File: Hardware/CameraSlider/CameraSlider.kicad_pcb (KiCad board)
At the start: 2 copper layers, 100 x 50 mm, 19 parts, among them J1 Screw_Terminal_01x02, J10 Conn_01x04_Male, J11 Conn_01x04_Male, J2 Conn_01x02_Male, J3 Conn_01x03_Male, J4 Conn_01x02_Male, J5 Conn_01x02_Male, J6 Conn_01x03_Male, J7 Conn_01x03_Male, J8 Conn_02x03_Odd_Even, J9 Conn_01x04_Male, U1 A000005, U2 A4988_STEPPER_MOTOR_DRIVER_CA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

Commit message: Layout hinzugefügt
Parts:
- moved C1 8.52 mm to (165.1, 119.4), turned to 0 degrees
- moved R1 2.54 mm to (156.2, 121.9)
- moved J3 1.27 mm to (116.8, 119.4)
- moved U1 1.27 mm to (128.3, 124.5)
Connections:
- U2 pad 11: Net-(J11-Pad2) -> Net-(J11-Pad3)
- U2 pad 12: Net-(J11-Pad1) -> Net-(J11-Pad4)
- U2 pad 13: Net-(J11-Pad3) -> Net-(J11-Pad2)
- U2 pad 14: Net-(J11-Pad4) -> Net-(J11-Pad1)
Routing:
- net +5V: track 0.00 -> 230.5 mm
- net +BATT: track 0.00 -> 49.0 mm, vias 0 -> 2
- net ENCODER_DT: track 0.00 -> 44.5 mm
- net X_DIR: track 0.00 -> 44.1 mm
- net Net-(J11-Pad3): track 0.00 -> 44.0 mm
- net Net-(J11-Pad4): track 0.00 -> 34.4 mm
- net ENCODER_CLK: track 0.00 -> 34.2 mm
- net Net-(J11-Pad2): track 0.00 -> 32.9 mm
- net Net-(J11-Pad1): track 0.00 -> 32.0 mm
- net EN: track 0.00 -> 25.4 mm, vias 0 -> 2
- net GND: track 0.00 -> 19.0 mm, vias 0 -> 13
- net X_STEP: track 0.00 -> 16.4 mm
- net ENDSTOP_LEFT: track 0.00 -> 13.8 mm
- net BUTTON_RIGHT: track 0.00 -> 12.6 mm
- net SDA: track 0.00 -> 9.42 mm
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- added copper zone on F.Cu, net GND
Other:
- board text added: "5V"
- board text added: "8-35V"
- board text added: "But L"
- board text added: "But R"
- board text added: "Enc"
- board text added: "End L"
- board text added: "End R"
- board text added: "OLED"
- board text added: "Stepper"

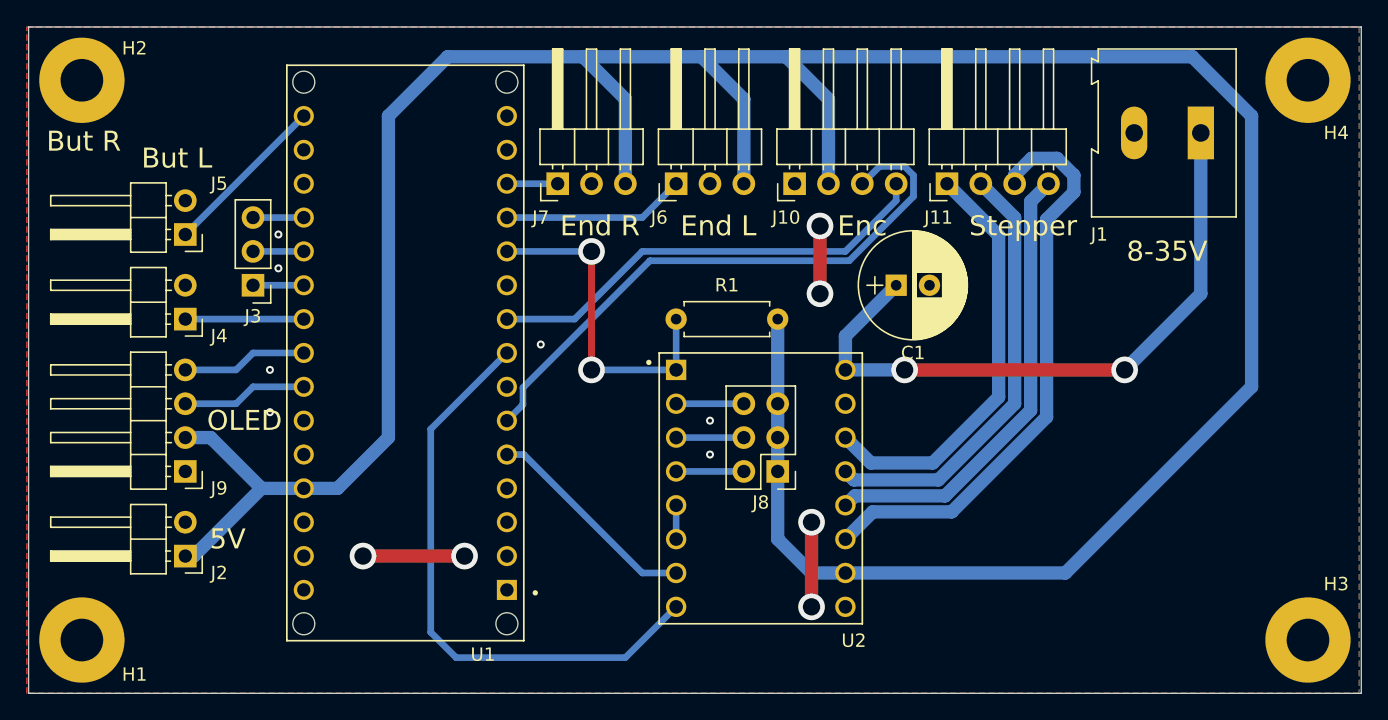
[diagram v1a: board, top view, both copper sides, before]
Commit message: Clearence vergrößert und GND Drahtbrücke hinzugefügt
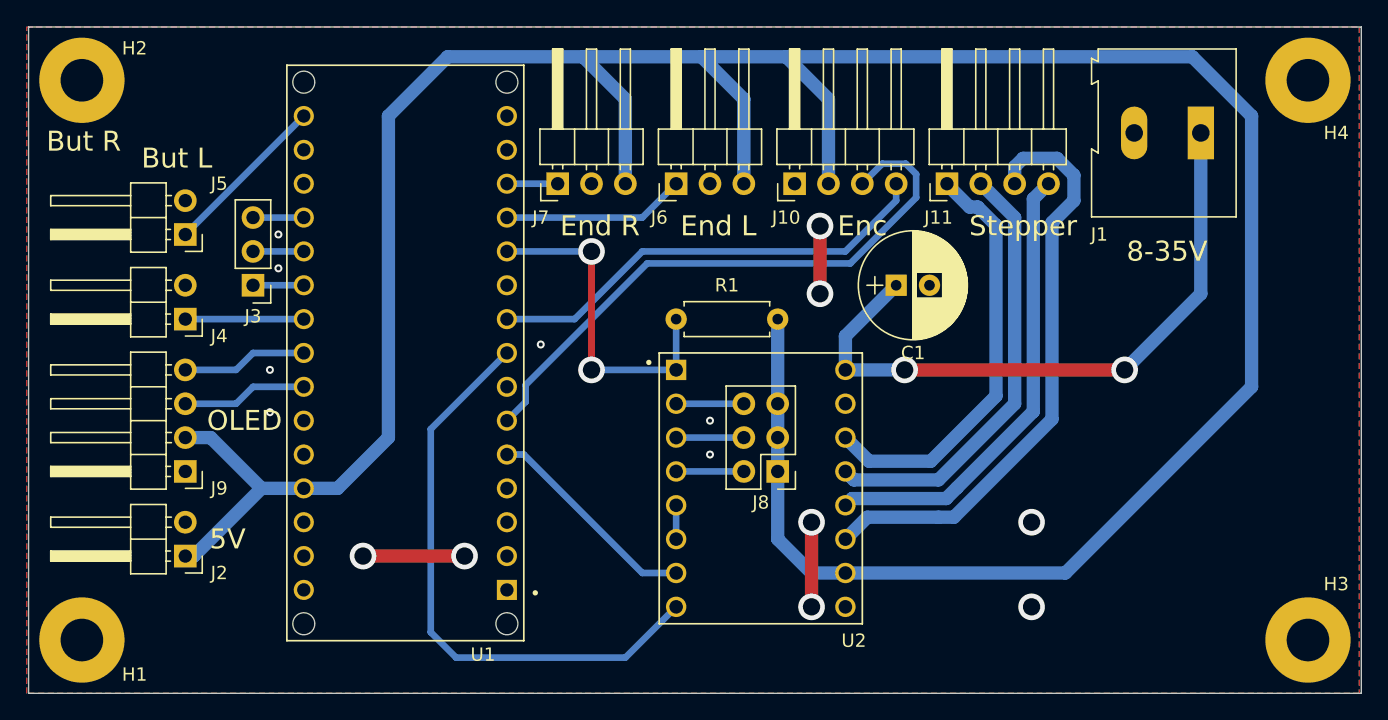
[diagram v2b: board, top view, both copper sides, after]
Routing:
- net Net-(J11-Pad3): track 44.0 -> 44.7 mm
- net ENCODER_DT: track 44.5 -> 45.1 mm
- net GND: vias 13 -> 15
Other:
- net class Default: clearance 0.2 -> 0.4
- rule trace_clearance: 0.2 -> 0.4
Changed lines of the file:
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@@
     (thickness 1.6)
     (drawings 13)
-    (tracks 124)
+    (tracks 131)
     (zones 0)
     (modules 19)
@@
     (user_trace_width 1)
     (user_trace_width 1.5)
-    (trace_clearance 0.2)
+    (trace_clearance 0.4)
     (zone_clearance 0.508)
     (zone_45_only no)
@@
   (net 25 "Net-(U2-Pad5)")
   (net_class Default "This is the default net class."
-    (clearance 0.2)
+    (clearance 0.4)
     (trace_width 0.25)
     (via_dia 0.8)
@@
   (segment (start 158.75 143.51) (end 158.75 137.16) (width 1) (layer F.Cu) (net 1))
   (segment (start 125.095 139.7) (end 132.715 139.7) (width 1) (layer F.Cu) (net 1))
+  (via (at 175.26 137.16) (size 2) (drill 1.3) (layers F.Cu B.Cu) (net 1))
+  (via (at 175.26 143.51) (size 2) (drill 1.3) (layers F.Cu B.Cu) (net 1))
   (segment (start 161.29 123.19) (end 165.1 119.38) (width 1) (layer B.Cu) (net 2))
   (segment (start 161.29 125.73) (end 161.29 123.19) (width 1) (layer B.Cu) (net 2))
@@
   (segment (start 116.84 127) (end 120.65 127) (width 0.5) (layer B.Cu) (net 15))
   (segment (start 115.57 128.27) (end 116.84 127) (width 0.5) (layer B.Cu) (net 15))
-  (segment (start 137.094001 127.065999) (end 146.61999 117.54001) (width 0.5) (layer B.Cu) (net 16))
-  (segment (start 137.094001 128.335999) (end 137.094001 127.065999) (width 0.5) (layer B.Cu) (net 16))
-  (segment (start 135.89 129.54) (end 137.094001 128.335999) (width 0.5) (layer B.Cu) (net 16))
-  (segment (start 165.724001 110.459999) (end 163.860001 110.459999) (width 0.5) (layer B.Cu) (net 16))
-  (segment (start 166.400001 111.135999) (end 165.724001 110.459999) (width 0.5) (layer B.Cu) (net 16))
-  (segment (start 166.400001 112.719962) (end 166.400001 111.135999) (width 0.5) (layer B.Cu) (net 16))
-  (segment (start 161.579953 117.54001) (end 166.400001 112.719962) (width 0.5) (layer B.Cu) (net 16))
-  (segment (start 163.860001 110.459999) (end 162.56 111.76) (width 0.5) (layer B.Cu) (net 16))
-  (segment (start 146.61999 117.54001) (end 161.579953 117.54001) (width 0.5) (layer B.Cu) (net 16))
+  (segment (start 165.820001 110.259999) (end 164.060001 110.259999) (width 0.5) (layer B.Cu) (net 16))
+  (segment (start 166.600001 111.039999) (end 165.820001 110.259999) (width 0.5) (layer B.Cu) (net 16))
+  (segment (start 164.060001 110.259999) (end 162.56 111.76) (width 0.5) (layer B.Cu) (net 16))
+  (segment (start 166.600001 112.802805) (end 166.600001 111.039999) (width 0.5) (layer B.Cu) (net 16))
+  (segment (start 161.662797 117.740009) (end 166.600001 112.802805) (width 0.5) (layer B.Cu) (net 16))
+  (segment (start 146.422796 117.74001) (end 161.662797 117.740009) (width 0.5) (layer B.Cu) (net 16))
+  (segment (start 137.294001 126.868805) (end 146.422796 117.74001) (width 0.5) (layer B.Cu) (net 16))
+  (segment (start 137.294001 128.135999) (end 137.294001 126.868805) (width 0.5) (layer B.Cu) (net 16))
+  (segment (start 135.89 129.54) (end 137.294001 128.135999) (width 0.5) (layer B.Cu) (net 16))
   (segment (start 135.89 121.92) (end 140.97 121.92) (width 0.5) (layer B.Cu) (net 17))
   (segment (start 140.97 121.92) (end 146.05 116.84) (width 0.5) (layer B.Cu) (net 17))
@@
   (segment (start 165.1 113.03) (end 165.1 111.76) (width 0.5) (layer B.Cu) (net 17))
   (segment (start 161.29 116.84) (end 165.1 113.03) (width 0.5) (layer B.Cu) (net 17))
-  (segment (start 175.19001 128.76706) (end 175.19001 113.09999) (width 1) (layer B.Cu) (net 18))
-  (segment (start 175.19001 113.09999) (end 176.53 111.76) (width 1) (layer B.Cu) (net 18))
-  (segment (start 168.772061 135.185009) (end 175.19001 128.76706) (width 1) (layer B.Cu) (net 18))
-  (segment (start 161.99499 135.18501) (end 168.772061 135.185009) (width 1) (layer B.Cu) (net 18))
-  (segment (start 161.29 135.89) (end 161.99499 135.18501) (width 1) (layer B.Cu) (net 18))
-  (segment (start 173.99 111.125) (end 173.99 111.76) (width 1) (layer B.Cu) (net 19))
-  (segment (start 175.26 109.855) (end 173.99 111.125) (width 1) (layer B.Cu) (net 19))
-  (segment (start 177.165 109.855) (end 175.26 109.855) (width 1) (layer B.Cu) (net 19))
-  (segment (start 178.435 111.125) (end 177.165 109.855) (width 1) (layer B.Cu) (net 19))
-  (segment (start 178.435 112.395) (end 178.435 111.125) (width 1) (layer B.Cu) (net 19))
-  (segment (start 176.39002 114.43998) (end 178.435 112.395) (width 1) (layer B.Cu) (net 19))
-  (segment (start 176.39002 129.26412) (end 176.39002 114.43998) (width 1) (layer B.Cu) (net 19))
-  (segment (start 169.269122 136.385018) (end 176.39002 129.26412) (width 1) (layer B.Cu) (net 19))
-  (segment (start 163.334982 136.385018) (end 169.269122 136.385018) (width 1) (layer B.Cu) (net 19))
-  (segment (start 161.29 138.43) (end 163.334982 136.385018) (width 1) (layer B.Cu) (net 19))
+  (segment (start 175.39001 112.89999) (end 176.53 111.76) (width 1) (layer B.Cu) (net 18))
+  (segment (start 175.39001 128.849903) (end 175.39001 112.89999) (width 1) (layer B.Cu) (net 18))
+  (segment (start 169.67501 134.564902) (end 175.39001 128.849903) (width 1) (layer B.Cu) (net 18))
+  (segment (start 168.854903 135.38501) (end 169.67501 134.564902) (width 1) (layer B.Cu) (net 18))
+  (segment (start 161.79499 135.38501) (end 168.854903 135.38501) (width 1) (layer B.Cu) (net 18))
+  (segment (start 161.29 135.89) (end 161.79499 135.38501) (width 1) (layer B.Cu) (net 18))
+  (segment (start 162.93498 136.78502) (end 161.29 138.43) (width 1) (layer B.Cu) (net 19))
+  (segment (start 176.79002 114.67498) (end 176.79002 129.429806) (width 1) (layer B.Cu) (net 19))
+  (segment (start 169.434807 136.785018) (end 168.275001 136.78502) (width 1) (layer B.Cu) (net 19))
+  (segment (start 178.435 113.03) (end 176.79002 114.67498) (width 1) (layer B.Cu) (net 19))
+  (segment (start 168.275001 136.78502) (end 162.93498 136.78502) (width 1) (layer B.Cu) (net 19))
+  (segment (start 178.435 111.125) (end 178.435 113.03) (width 1) (layer B.Cu) (net 19))
+  (segment (start 177.165 109.855) (end 178.435 111.125) (width 1) (layer B.Cu) (net 19))
+  (segment (start 176.79002 129.429806) (end 169.434807 136.785018) (width 1) (layer B.Cu) (net 19))
+  (segment (start 174.625 109.855) (end 177.165 109.855) (width 1) (layer B.Cu) (net 19))
+  (segment (start 173.99 110.49) (end 174.625 109.855) (width 1) (layer B.Cu) (net 19))
+  (segment (start 173.99 111.76) (end 173.99 110.49) (width 1) (layer B.Cu) (net 19))
   (segment (start 173.99 114.3) (end 171.45 111.76) (width 1) (layer B.Cu) (net 20))
   (segment (start 173.99 128.27) (end 173.99 114.3) (width 1) (layer B.Cu) (net 20))
@@
   (segment (start 161.925 133.985) (end 168.275 133.985) (width 1) (layer B.Cu) (net 20))
   (segment (start 161.29 133.35) (end 161.925 133.985) (width 1) (layer B.Cu) (net 20))
-  (segment (start 161.29 130.81) (end 163.195 132.715) (width 1) (layer B.Cu) (net 21))
-  (segment (start 163.195 132.715) (end 167.84793 132.715) (width 1) (layer B.Cu) (net 21))
-  (segment (start 167.84793 132.715) (end 172.78999 127.77294) (width 1) (layer B.Cu) (net 21))
-  (segment (start 172.78999 115.63999) (end 168.91 111.76) (width 1) (layer B.Cu) (net 21))
-  (segment (start 172.78999 127.77294) (end 172.78999 115.63999) (width 1) (layer B.Cu) (net 21))
+  (segment (start 161.29 130.81) (end 163.06499 132.58499) (width 1) (layer B.Cu) (net 21))
+  (segment (start 163.06499 132.58499) (end 167.695098 132.58499) (width 1) (layer B.Cu) (net 21))
+  (segment (start 167.695098 132.58499) (end 172.58999 127.690098) (width 1) (layer B.Cu) (net 21))
+  (segment (start 172.58999 127.690098) (end 172.58999 114.879902) (width 1) (layer B.Cu) (net 21))
+  (segment (start 172.58999 114.879902) (end 171.220089 113.510001) (width 1) (layer B.Cu) (net 21))
+  (segment (start 168.91 111.810002) (end 168.91 111.76) (width 1) (layer B.Cu) (net 21))
+  (segment (start 170.609999 113.510001) (end 168.91 111.810002) (width 1) (layer B.Cu) (net 21))
+  (segment (start 171.220089 113.510001) (end 170.609999 113.510001) (width 1) (layer B.Cu) (net 21))
   (segment (start 148.59 125.73) (end 148.59 121.92) (width 0.5) (layer B.Cu) (net 22))
   (segment (start 142.24 125.73) (end 148.59 125.73) (width 0.5) (layer B.Cu) (net 22))
